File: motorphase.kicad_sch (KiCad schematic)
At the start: 9 parts, among them J4 Motor Connection, Q1 CSD88584Q5DCT

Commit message: before big shunt:
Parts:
- removed R1: 0.02R, Resistor_SMD:R_0805_2012Metric, symbol Device:R_Small_US
- added C12: 10nF, Capacitor_SMD:C_0402_1005Metric, symbol Device:C_Small
- added C13: 4.7nF, Capacitor_SMD:C_0402_1005Metric, symbol Device:C_Small
- added C18: 1nF, symbol Device:C_Small
- added R1: WFCP06124L000FE66 0.004R, RESC2550X76N, symbol O32controller:WFCP06124L000FE66
- added R23: 2.21R, Resistor_SMD:R_0402_1005Metric, symbol Device:R_Small_US
- R2, R3: value R_Small_US -> 1.78k
- R4: value R_Small_US -> 13.7k
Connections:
- net GND: now also R1.1, R23.2
- net Motor: now also C13.1
- net OP_N: now also C18.1
- net OP_O: now also C18.2
- net VBUS: now also C12.1
- net Sense_P renamed SENSE_P
- net SENSE_P: now also C12.2, R1.2
- new net: C13.2, R23.1
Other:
- note added: "2.2RC = 4us"
- note added: "Gain ≈ 1+Rn/Rf https://www.desmos.com/calculator/xwloujyche"
- note removed: "Gain = 1+Rn/Rf"
- moved on the sheet: NT1, R2, R3, R4

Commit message: used 2512 shunts to bridge vias
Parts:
- R1: footprint RESC2550X76N -> Resistor_SMD:R_Shunt_2512_6332Metric
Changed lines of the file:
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@@
       (effects (font (size 1.27 1.27)) (justify left))
     )
-    (property "Footprint" "RESC2550X76N" (id 2) (at 128.27 134.62 0)
+    (property "Footprint" "Resistor_SMD:R_Shunt_2512_6332Metric" (id 2) (at 128.27 134.62 0)
       (effects (font (size 1.27 1.27)) (justify bottom) hide)
     )

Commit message: routed some more
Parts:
- R23: value 2.21R -> 2.2R
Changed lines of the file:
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@@
       (effects (font (size 1.27 1.27)) (justify left))
     )
-    (property "Value" "2.21R" (id 1) (at 148.59 97.79 0)
+    (property "Value" "2.2R" (id 1) (at 148.59 97.79 0)
       (effects (font (size 1.27 1.27)) (justify left))
     )
@@
       (effects (font (size 1.27 1.27)) hide)
     )
-    (property "Datasheet" "~" (id 3) (at 146.05 96.52 0)
+    (property "Datasheet" "https://www.digikey.com/en/products/detail/koa-speer-electronics-inc/SG73P1ETTP2R20F/10188311" (id 3) (at 146.05 96.52 0)
       (effects (font (size 1.27 1.27)) hide)
     )

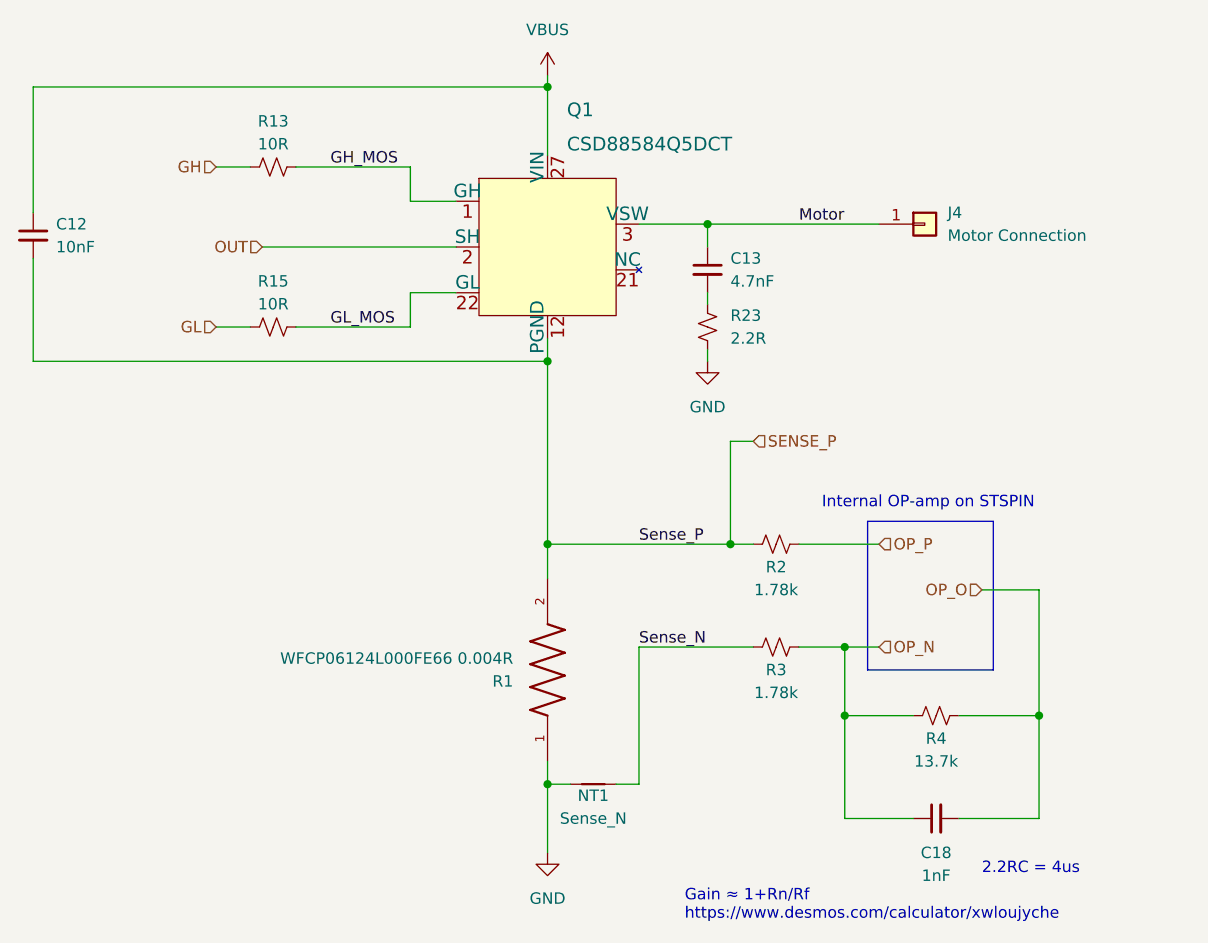
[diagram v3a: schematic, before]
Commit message: routed some sense, netties, fixed NC
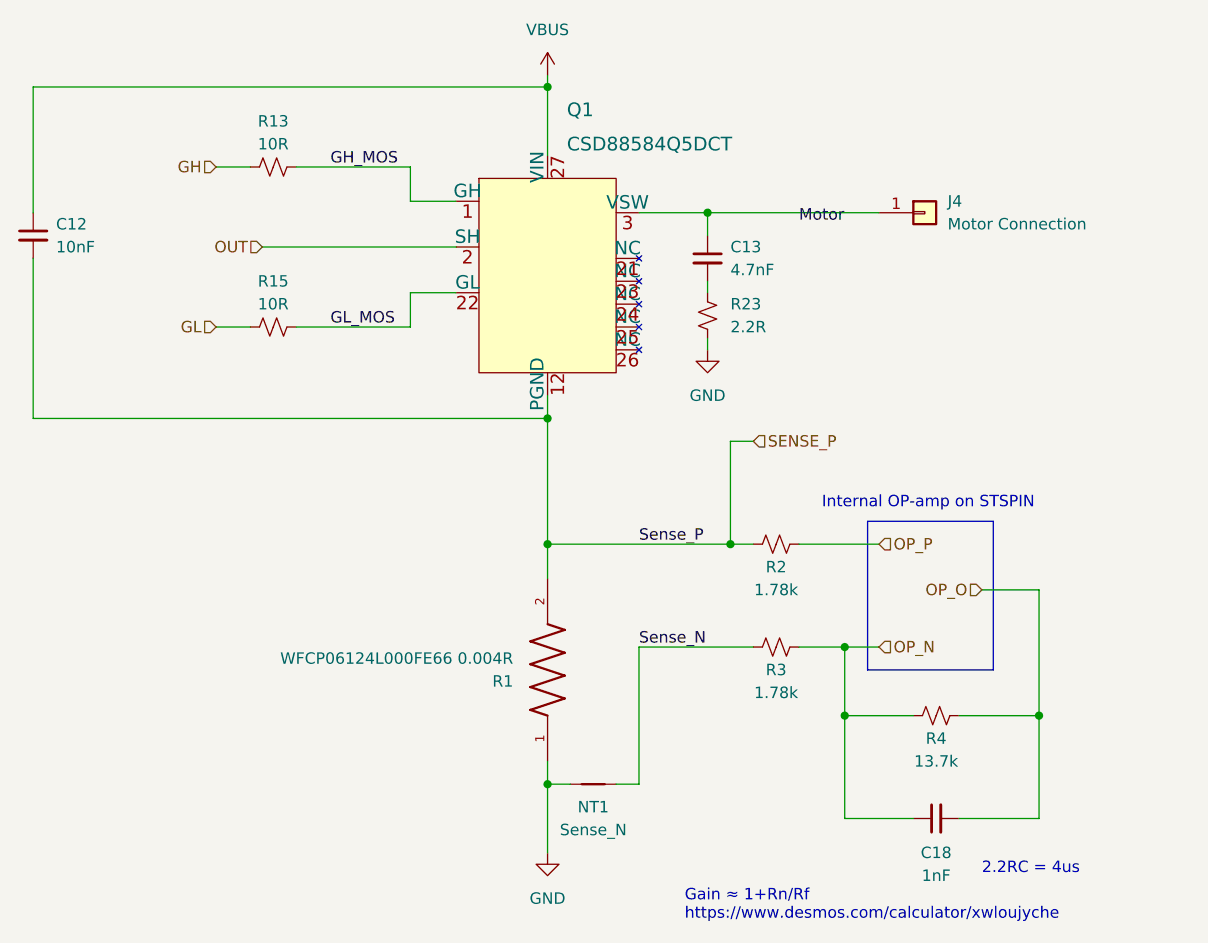
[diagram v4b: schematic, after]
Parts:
- C18: footprint (none) -> Capacitor_SMD:C_0402_1005Metric
- NT1: footprint (none) -> NetTie:NetTie-small
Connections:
- net Motor: no longer C13.1, J4.1 (Pin_1), Q1.3 (VSW)
- new net: C13.1, J4.1 (Pin_1), Q1.3 (VSW)
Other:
- moved on the sheet: C13, J4, R23
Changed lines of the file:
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@@
   (junction (at 161.29 132.08) (diameter 0) (color 0 0 0 0)
   )
-  (junction (at 128.27 100.33) (diameter 0) (color 0 0 0 0)
+  (junction (at 128.27 106.68) (diameter 0) (color 0 0 0 0)
   )
   (junction (at 161.29 139.7) (diameter 0) (color 0 0 0 0)
   )
-  (junction (at 146.05 85.09) (diameter 0) (color 0 0 0 0)
+  (junction (at 146.05 83.82) (diameter 0) (color 0 0 0 0)
   )
   (junction (at 128.27 147.32) (diameter 0) (color 0 0 0 0)
@@
     (stroke (width 0) (type default) (color 0 0 0 0))
   )
-  (wire (pts (xy 138.43 85.09) (xy 146.05 85.09))
+  (wire (pts (xy 138.43 83.82) (xy 146.05 83.82))
     (stroke (width 0) (type default) (color 0 0 0 0))
   )
@@
     (stroke (width 0) (type default) (color 0 0 0 0))
   )
+  (wire (pts (xy 128.27 106.68) (xy 128.27 120.65))
+    (stroke (width 0) (type default) (color 0 0 0 0))
+  )
   (wire (pts (xy 173.99 151.13) (xy 182.88 151.13))
     (stroke (width 0) (type default) (color 0 0 0 0))
@@
     (stroke (width 0) (type default) (color 0 0 0 0))
   )
-  (wire (pts (xy 128.27 100.33) (xy 128.27 120.65))
-    (stroke (width 0) (type default) (color 0 0 0 0))
-  )
-  (wire (pts (xy 146.05 85.09) (xy 165.1 85.09))
+  (wire (pts (xy 146.05 83.82) (xy 165.1 83.82))
     (stroke (width 0) (type default) (color 0 0 0 0))
   )
@@
     (stroke (width 0) (type default) (color 0 0 0 0))
   )
-  (wire (pts (xy 71.12 100.33) (xy 71.12 88.9))
+  (wire (pts (xy 71.12 106.68) (xy 71.12 88.9))
     (stroke (width 0) (type default) (color 0 0 0 0))
   )
@@
     (stroke (width 0) (type default) (color 0 0 0 0))
   )
-  (wire (pts (xy 146.05 92.71) (xy 146.05 93.98))
+  (wire (pts (xy 146.05 91.44) (xy 146.05 92.71))
     (stroke (width 0) (type default) (color 0 0 0 0))
   )
@@
     (stroke (width 0) (type default) (color 0 0 0 0))
   )
-  (wire (pts (xy 146.05 100.33) (xy 146.05 99.06))
+  (wire (pts (xy 146.05 99.06) (xy 146.05 97.79))
     (stroke (width 0) (type default) (color 0 0 0 0))
   )
@@
     (stroke (width 0) (type default) (color 0 0 0 0))
   )
+  (wire (pts (xy 128.27 104.14) (xy 128.27 106.68))
+    (stroke (width 0) (type default) (color 0 0 0 0))
+  )
   (polyline (pts (xy 177.8 134.62) (xy 177.8 118.11))
     (stroke (width 0) (type default) (color 0 0 0 0))
   )
-  (wire (pts (xy 128.27 97.79) (xy 128.27 100.33))
-    (stroke (width 0) (type default) (color 0 0 0 0))
-  )
   (wire (pts (xy 128.27 120.65) (xy 128.27 124.46))
     (stroke (width 0) (type default) (color 0 0 0 0))
@@
     (stroke (width 0) (type default) (color 0 0 0 0))
   )
-  (wire (pts (xy 128.27 100.33) (xy 71.12 100.33))
+  (wire (pts (xy 128.27 106.68) (xy 71.12 106.68))
     (stroke (width 0) (type default) (color 0 0 0 0))
   )
@@
     (stroke (width 0) (type default) (color 0 0 0 0))
   )
-  (wire (pts (xy 146.05 87.63) (xy 146.05 85.09))
+  (wire (pts (xy 146.05 86.36) (xy 146.05 83.82))
     (stroke (width 0) (type default) (color 0 0 0 0))
   )
@@
     (pin "1")
   )
-  (symbol (lib_id "Device:R_Small_US") (at 146.05 96.52 0) (unit 1)
-    (in_bom yes) (on_board yes)
-    (property "Reference" "R23" (id 0) (at 148.59 95.25 0)
-      (effects (font (size 1.27 1.27)) (justify left))
-    )
-    (property "Value" "2.2R" (id 1) (at 148.59 97.79 0)
-      (effects (font (size 1.27 1.27)) (justify left))
-    )
-    (property "Footprint" "Resistor_SMD:R_0402_1005Metric" (id 2) (at 146.05 96.52 0)
-      (effects (font (size 1.27 1.27)) hide)
-    )
-    (property "Datasheet" "https://www.digikey.com/en/products/detail/koa-speer-electronics-inc/SG73P1ETTP2R20F/10188311" (id 3) (at 146.05 96.52 0)
+  (symbol (lib_id "Device:R_Small_US") (at 146.05 95.25 0) (unit 1)
+    (in_bom yes) (on_board yes)
+    (property "Reference" "R23" (id 0) (at 148.59 93.98 0)
+      (effects (font (size 1.27 1.27)) (justify left))
+    )
+    (property "Value" "2.2R" (id 1) (at 148.59 96.52 0)
+      (effects (font (size 1.27 1.27)) (justify left))
+    )
+    (property "Footprint" "Resistor_SMD:R_0402_1005Metric" (id 2) (at 146.05 95.25 0)
+      (effects (font (size 1.27 1.27)) hide)
+    )
+    (property "Datasheet" "https://www.digikey.com/en/products/detail/koa-speer-electronics-inc/SG73P1ETTP2R20F/10188311" (id 3) (at 146.05 95.25 0)
       (effects (font (size 1.27 1.27)) hide)
     )
@@
     (pin "1")
   )
-  (symbol (lib_id "Device:C_Small") (at 146.05 90.17 0) (unit 1)
-    (in_bom yes) (on_board yes)
-    (property "Reference" "C13" (id 0) (at 148.59 88.9 0)
-      (effects (font (size 1.27 1.27)) (justify left))
-    )
-    (property "Value" "4.7nF" (id 1) (at 148.59 91.4462 0)
-      (effects (font (size 1.27 1.27)) (justify left))
-    )
-    (property "Footprint" "Capacitor_SMD:C_0402_1005Metric" (id 2) (at 146.05 90.17 0)
-      (effects (font (size 1.27 1.27)) hide)
-    )
-    (property "Datasheet" "~" (id 3) (at 146.05 90.17 0)
+  (symbol (lib_id "Device:C_Small") (at 146.05 88.9 0) (unit 1)
+    (in_bom yes) (on_board yes)
+    (property "Reference" "C13" (id 0) (at 148.59 87.63 0)
+      (effects (font (size 1.27 1.27)) (justify left))
+    )
+    (property "Value" "4.7nF" (id 1) (at 148.59 90.1762 0)
+      (effects (font (size 1.27 1.27)) (justify left))
+    )
+    (property "Footprint" "Capacitor_SMD:C_0402_1005Metric" (id 2) (at 146.05 88.9 0)
+      (effects (font (size 1.27 1.27)) hide)
+    )
+    (property "Datasheet" "~" (id 3) (at 146.05 88.9 0)
       (effects (font (size 1.27 1.27)) hide)
     )
@@
   (symbol (lib_id "Device:NetTie_2") (at 133.35 147.32 180) (unit 1)
     (in_bom yes) (on_board yes)
-    (property "Reference" "NT1" (id 0) (at 133.35 148.59 0))
-    (property "Value" "Sense_N" (id 1) (at 133.35 151.13 0))
-    (property "Footprint" "" (id 2) (at 133.35 147.32 0)
+    (property "Reference" "NT1" (id 0) (at 133.35 149.86 0))
+    (property "Value" "Sense_N" (id 1) (at 133.35 152.4 0))
+    (property "Footprint" "NetTie:NetTie-small" (id 2) (at 133.35 147.32 0)
       (effects (font (size 1.27 1.27)) hide)
     )
@@
     (pin "2")
   )
-  (symbol (lib_id "power:GND") (at 146.05 100.33 0) (unit 1)
-    (in_bom yes) (on_board yes) (fields_autoplaced)
-    (property "Reference" "#PWR0115" (id 0) (at 146.05 106.68 0)
-      (effects (font (size 1.27 1.27)) hide)
-    )
-    (property "Value" "GND" (id 1) (at 146.05 105.41 0))
-    (property "Footprint" "" (id 2) (at 146.05 100.33 0)
-      (effects (font (size 1.27 1.27)) hide)
-    )
-    (property "Datasheet" "" (id 3) (at 146.05 100.33 0)
-      (effects (font (size 1.27 1.27)) hide)
-    )
-    (pin "1")
-  )
-  (symbol (lib_id "Connector_Generic:Conn_01x01") (at 170.18 85.09 0) (unit 1)
-    (in_bom yes) (on_board yes) (fields_autoplaced)
-    (property "Reference" "J4" (id 0) (at 172.72 83.8199 0)
-      (effects (font (size 1.27 1.27)) (justify left))
-    )
-    (property "Value" "Motor Connection" (id 1) (at 172.72 86.3599 0)
-      (effects (font (size 1.27 1.27)) (justify left))
-    )
-    (property "Footprint" "O32controller:SolderWire-Actual_1x01_D1.7mm_OD_2.75mm" (id 2) (at 170.18 85.09 0)
-      (effects (font (size 1.27 1.27)) hide)
-    )
-    (property "Datasheet" "~" (id 3) (at 170.18 85.09 0)
+  (symbol (lib_id "power:GND") (at 146.05 99.06 0) (unit 1)
+    (in_bom yes) (on_board yes) (fields_autoplaced)
+    (property "Reference" "#PWR0115" (id 0) (at 146.05 105.41 0)
+      (effects (font (size 1.27 1.27)) hide)
+    )
+    (property "Value" "GND" (id 1) (at 146.05 104.14 0))
+    (property "Footprint" "" (id 2) (at 146.05 99.06 0)
+      (effects (font (size 1.27 1.27)) hide)
+    )
+    (property "Datasheet" "" (id 3) (at 146.05 99.06 0)
+      (effects (font (size 1.27 1.27)) hide)
+    )
+    (pin "1")
+  )
+  (symbol (lib_id "Connector_Generic:Conn_01x01") (at 170.18 83.82 0) (unit 1)
+    (in_bom yes) (on_board yes) (fields_autoplaced)
+    (property "Reference" "J4" (id 0) (at 172.72 82.5499 0)
+      (effects (font (size 1.27 1.27)) (justify left))
+    )
+    (property "Value" "Motor Connection" (id 1) (at 172.72 85.0899 0)
+      (effects (font (size 1.27 1.27)) (justify left))
+    )
+    (property "Footprint" "O32controller:SolderWire-Actual_1x01_D1.7mm_OD_2.75mm" (id 2) (at 170.18 83.82 0)
+      (effects (font (size 1.27 1.27)) hide)
+    )
+    (property "Datasheet" "~" (id 3) (at 170.18 83.82 0)
       (effects (font (size 1.27 1.27)) hide)
     )
@@
     (property "Reference" "C18" (id 0) (at 171.45 154.94 90))
     (property "Value" "1nF" (id 1) (at 171.45 157.48 90))
-    (property "Footprint" "" (id 2) (at 171.45 151.13 0)
+    (property "Footprint" "Capacitor_SMD:C_0402_1005Metric" (id 2) (at 171.45 151.13 0)
       (effects (font (size 1.27 1.27)) hide)
     )
@@
     (pin "21")
     (pin "22")
+    (pin "23")
+    (pin "24")
+    (pin "25")
+    (pin "26")
     (pin "27")
     (pin "3")

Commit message: trying to fix shunt footprint:
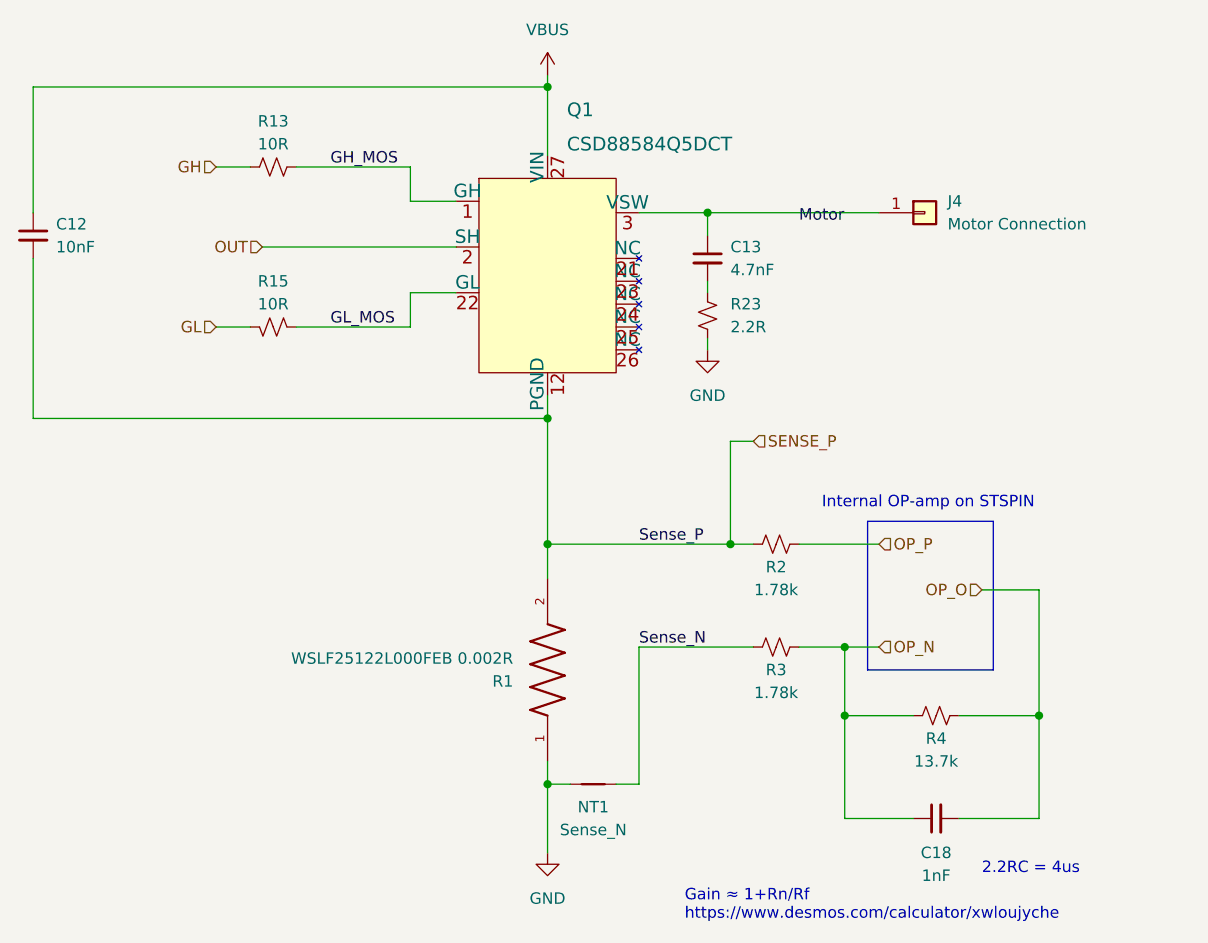
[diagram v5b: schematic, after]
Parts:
- R1: value WFCP06124L000FE66 0.004R -> WSLF25122L000FEB 0.002R; footprint Resistor_SMD:R_Shunt_2512_6332Metric -> (none); symbol O32controller:WFCP06124L000FE66 -> O32controller:WSLF25122L000FEB
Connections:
- net GL: now also R15.2; no longer R15.1
- net GL_MOS: now also R15.1; no longer R15.2
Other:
- moved on the sheet: R15
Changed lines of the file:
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@@
     (pin "2")
   )
-  (symbol (lib_id "Device:R_Small_US") (at 97.79 96.52 90) (unit 1)
+  (symbol (lib_id "Device:R_Small_US") (at 97.79 96.52 270) (mirror x) (unit 1)
     (in_bom yes) (on_board yes)
     (property "Reference" "R15" (id 0) (at 97.79 91.44 90))
@@
     (pin "3")
   )
-  (symbol (lib_id "O32controller:WFCP06124L000FE66") (at 128.27 134.62 90) (unit 1)
+  (symbol (lib_id "O32controller:WSLF25122L000FEB") (at 128.27 134.62 90) (unit 1)
     (in_bom yes) (on_board yes)
     (property "Reference" "R1" (id 0) (at 124.46 135.8901 90)
       (effects (font (size 1.27 1.27)) (justify left))
     )
-    (property "Value" "WFCP06124L000FE66 0.004R" (id 1) (at 124.46 133.3501 90)
-      (effects (font (size 1.27 1.27)) (justify left))
-    )
-    (property "Footprint" "Resistor_SMD:R_Shunt_2512_6332Metric" (id 2) (at 128.27 134.62 0)
+    (property "Value" "WSLF25122L000FEB 0.002R" (id 1) (at 124.46 133.3501 90)
+      (effects (font (size 1.27 1.27)) (justify left))
+    )
+    (property "Footprint" "" (id 2) (at 128.27 134.62 0)
       (effects (font (size 1.27 1.27)) (justify bottom) hide)
     )

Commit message: routed more signals
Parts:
- R1: footprint (none) -> Resistor_SMD:R_Shunt_2512_6332Metric
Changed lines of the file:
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@@
       (effects (font (size 1.27 1.27)) (justify left))
     )
-    (property "Footprint" "" (id 2) (at 128.27 134.62 0)
+    (property "Footprint" "Resistor_SMD:R_Shunt_2512_6332Metric" (id 2) (at 128.27 134.62 0)
       (effects (font (size 1.27 1.27)) (justify bottom) hide)
     )

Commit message: i don't like CAN
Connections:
- net Motor: now also C13.1, J4.1 (Pin_1), Q1.3 (VSW)
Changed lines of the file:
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@@
     (effects (font (size 1.27 1.27)) (justify left bottom))
   )
-  (label "Motor" (at 156.21 85.09 0)
+  (label "Motor" (at 156.21 83.82 0)
     (effects (font (size 1.27 1.27)) (justify left bottom))
   )

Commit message: added mag702, leds, thought about tx out:
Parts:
- R1: footprint Resistor_SMD:R_Shunt_2512_6332Metric -> RESC2550X76N
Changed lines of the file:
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@@
       (effects (font (size 1.27 1.27)) hide)
     )
-    (property "Datasheet" "https://www.digikey.com/en/products/detail/koa-speer-electronics-inc/SG73P1ETTP2R20F/10188311" (id 3) (at 146.05 95.25 0)
+    (property "Datasheet" "~" (id 3) (at 146.05 95.25 0)
       (effects (font (size 1.27 1.27)) hide)
     )
@@
       (effects (font (size 1.27 1.27)) (justify left))
     )
-    (property "Footprint" "Resistor_SMD:R_Shunt_2512_6332Metric" (id 2) (at 128.27 134.62 0)
+    (property "Footprint" "RESC2550X76N" (id 2) (at 128.27 134.62 0)
       (effects (font (size 1.27 1.27)) (justify bottom) hide)
     )
